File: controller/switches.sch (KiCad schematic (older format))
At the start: 38 parts, among them J10 Conn_01x03, J11 Conn_01x03, J12 Conn_01x02, J13 Conn_01x04, J14 Conn_01x04, J8 Conn_01x08, J9 Conn_01x08, SW1 SW_SPDT_MSM, SW10 SW_Push, SW11 SW_DP3T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

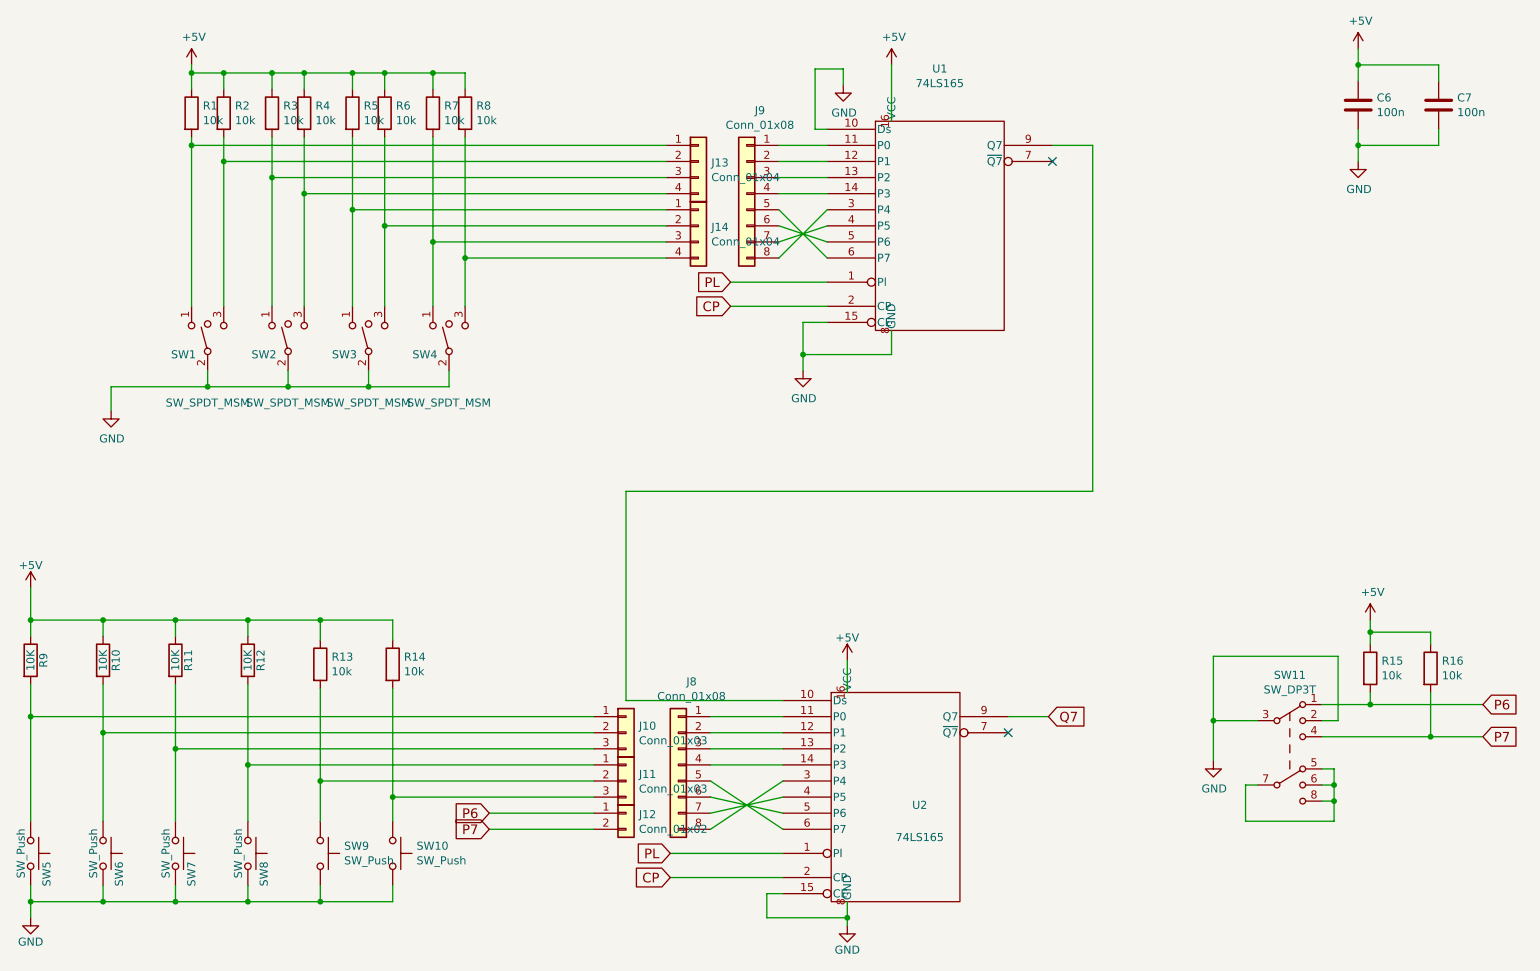
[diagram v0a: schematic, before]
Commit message: Update to 4-pin I2C display.
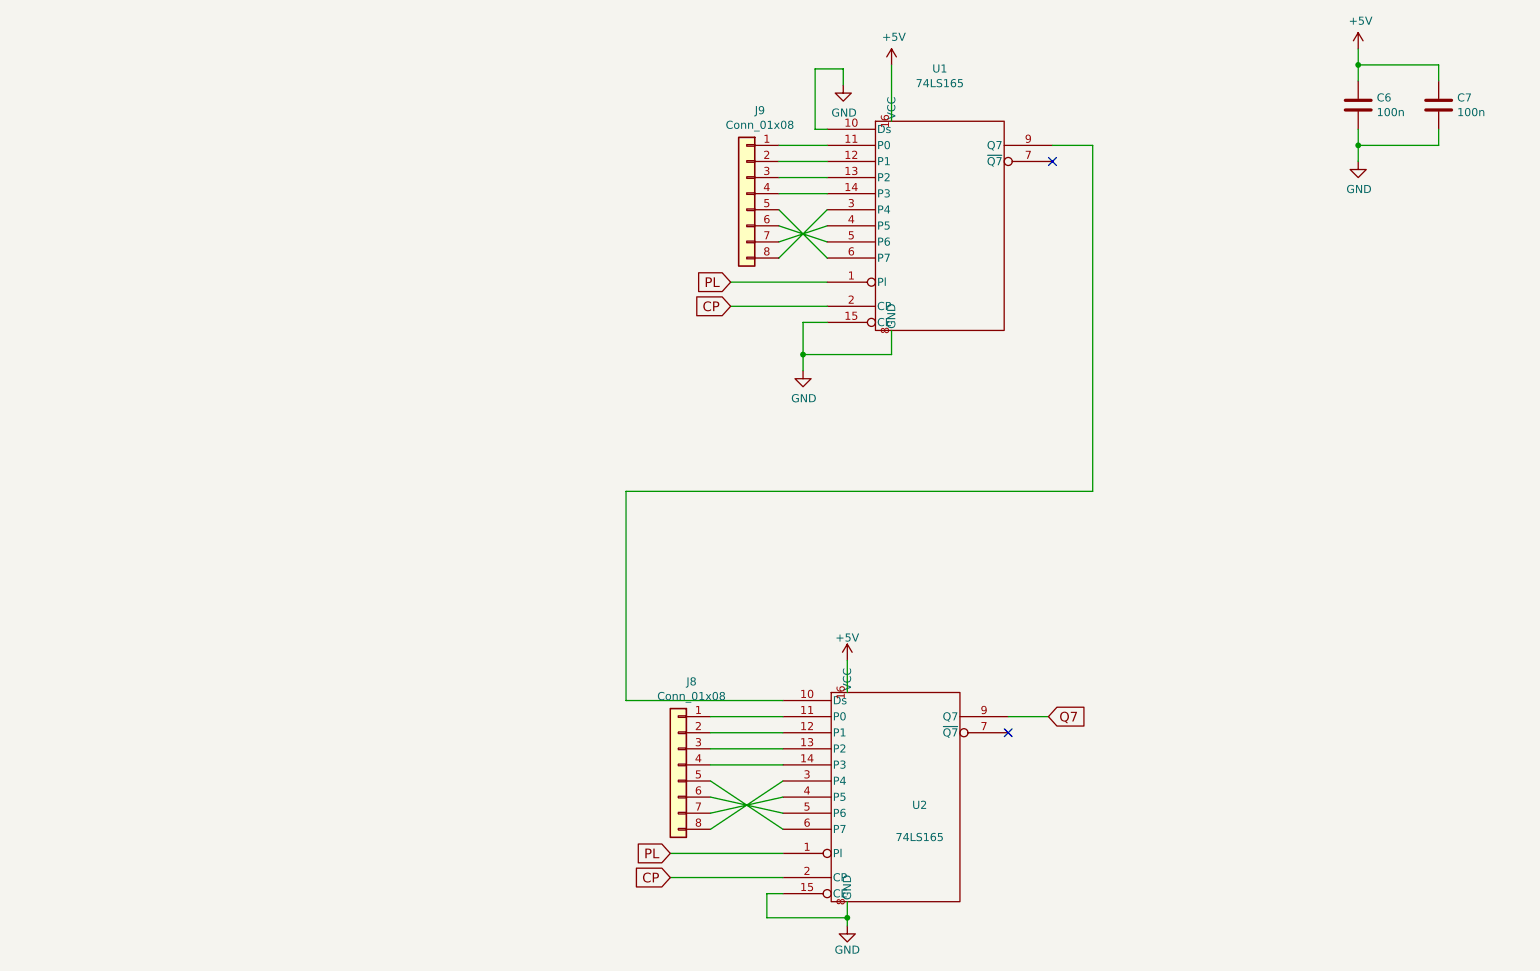
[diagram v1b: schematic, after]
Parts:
- removed J10, J11: Conn_01x03, Milling:JST_XH_B03B-XH-A_1x03_P2.50mm_Vertical_Milling, symbol Connector_Generic:Conn_01x03
- removed J12: Conn_01x02, Milling:JST_XH_B02B-XH-A_1x02_P2.50mm_Vertical_Milling, symbol Connector_Generic:Conn_01x02
- removed J13, J14: Conn_01x04, Milling:JST_XH_B04B-XH-A_1x04_P2.50mm_Vertical_Milling, symbol Connector_Generic:Conn_01x04
- removed R1, R13, R14, R15, R16, R2, R3, R4, R5, R6, R7, R8: 10k, Resistor_SMD:R_0805_2012Metric, symbol Device:R
- removed R10, R11, R12, R9: 10K, Resistor_SMD:R_0805_2012Metric, symbol remote-rescue:R
- removed SW1, SW2, SW3, SW4: SW_SPDT_MSM, Remote:Switch_1x03_P5.08mm, symbol remote-rescue:SW_SPDT_MSM
- removed SW10, SW5, SW6, SW7, SW8, SW9: SW_Push, Remote:Switch_1x02_P6mm, symbol remote-rescue:SW_Push
- removed SW11: SW_DP3T, Remote:Switch_2x03_P3mm_Slide, symbol remote:SW_DP3T
